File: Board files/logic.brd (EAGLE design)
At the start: 44.5 x 57.1 mm, 21 parts, among them U1 LD1117, U2 LM2662, U3 LD1085V

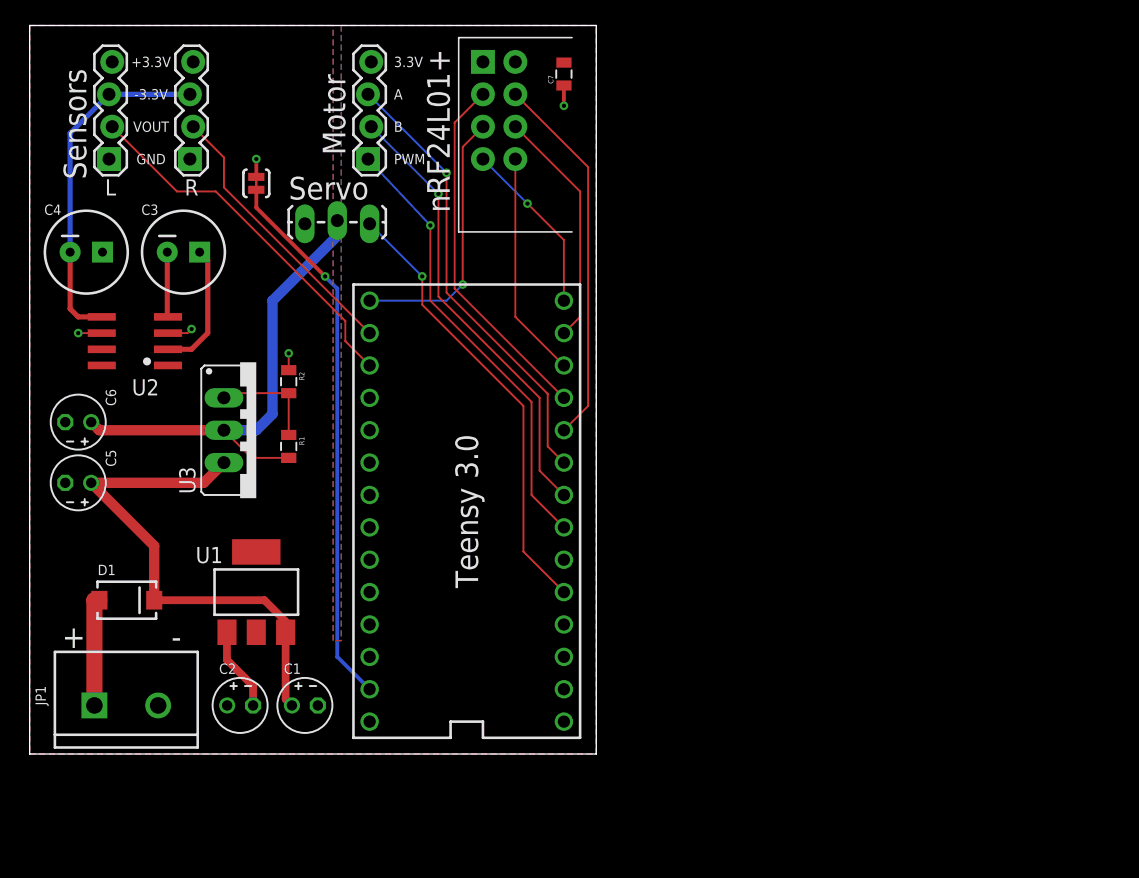
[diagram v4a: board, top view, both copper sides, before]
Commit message: Labels are no longer obscured by vias
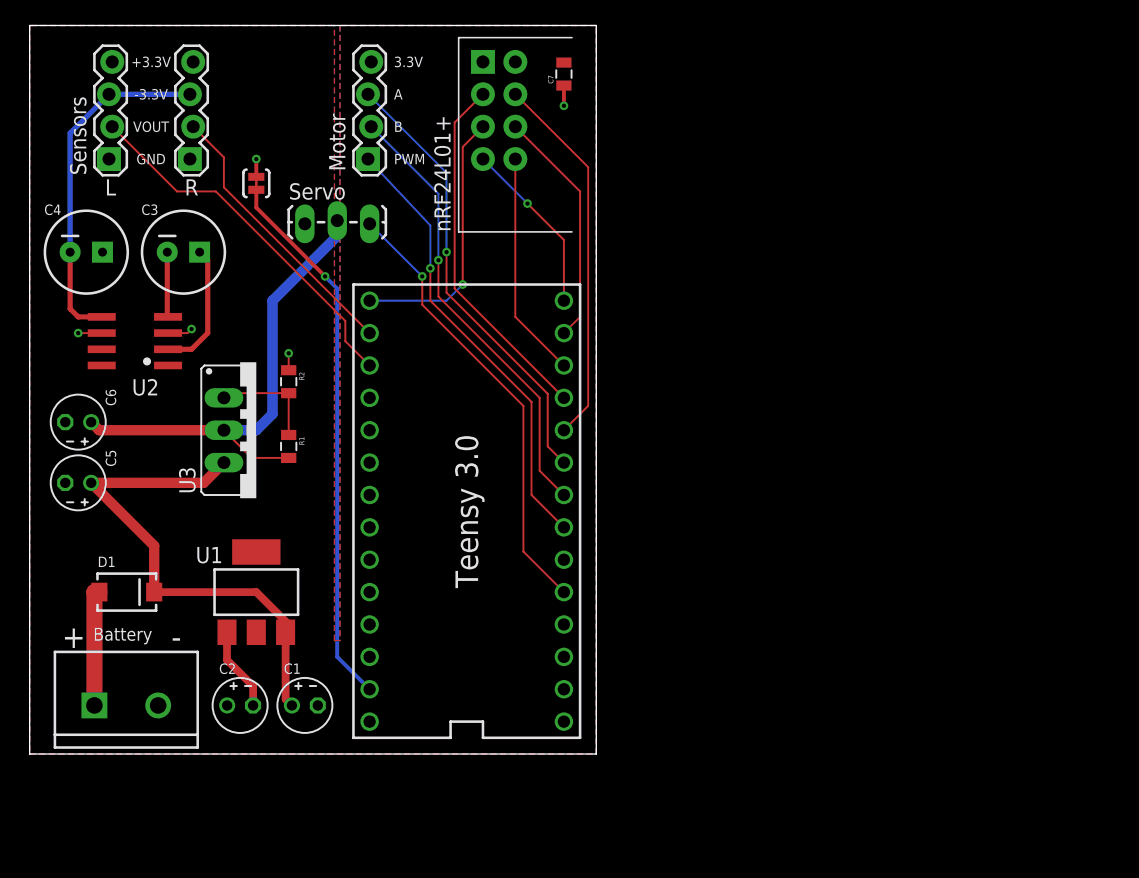
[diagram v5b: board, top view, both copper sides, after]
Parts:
- moved D1 0.63 mm to (7.62, 12.7)
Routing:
- net N$1: track 8.64 -> 9.28 mm
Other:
- board text added: "Battery"
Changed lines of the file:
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@@
 <text x="11.1125" y="9.2075" size="1.778" layer="21" align="center-left">-</text>
 <text x="34.29" y="19.05" size="1.778" layer="21" rot="R90" align="center">Teensy 3.0</text>
-<text x="32.0675" y="48.895" size="1.778" layer="21" rot="R90" align="center">nRF24L01+</text>
+<text x="33.02" y="40.9575" size="1.27" layer="21" rot="R90">nRF24L01+</text>
 <text x="9.525" y="46.6725" size="0.8128" layer="21" align="center">GND</text>
 <text x="9.525" y="49.2125" size="0.8128" layer="21" align="center">VOUT</text>
 <text x="9.525" y="51.7525" size="0.8128" layer="21" align="center">-3.3V</text>
 <text x="9.525" y="54.2925" size="0.8128" layer="21" align="center">+3.3V</text>
-<text x="4.445" y="45.085" size="1.778" layer="21" rot="R90">Sensors</text>
-<text x="20.32" y="43.4975" size="1.778" layer="21">Servo</text>
-<text x="24.765" y="46.99" size="1.778" layer="21" rot="R90">Motor</text>
+<text x="4.445" y="45.4025" size="1.27" layer="21" rot="R90">Sensors</text>
+<text x="20.32" y="43.4975" size="1.27" layer="21">Servo</text>
+<text x="24.765" y="45.72" size="1.27" layer="21" rot="R90">Motor</text>
 <text x="6.35" y="45.085" size="1.27" layer="21" align="top-center">L</text>
 <text x="12.7" y="45.085" size="1.27" layer="21" align="top-center">R</text>
+<text x="7.3025" y="8.89" size="1.016" layer="21" align="bottom-center">Battery</text>
 </plain>
 <attributes>
@@
 </autorouter>
 <elements>
-<element name="D1" library="SparkFun-DiscreteSemi" package="SMA-DIODE" value="" x="7.62" y="12.065" smashed="yes">
-<attribute name="NAME" x="5.334" y="14.0335" size="0.8128" layer="25"/>
-<attribute name="VALUE" x="7.874" y="13.716" size="0.4064" layer="27"/>
+<element name="D1" library="SparkFun-DiscreteSemi" package="SMA-DIODE" value="" x="7.62" y="12.7" smashed="yes">
+<attribute name="NAME" x="5.334" y="14.6685" size="0.8128" layer="25"/>
+<attribute name="VALUE" x="7.874" y="14.351" size="0.4064" layer="27"/>
 </element>
 <element name="U1" library="Custom" package="SOT-223" value="LD1117" x="17.78" y="12.7" smashed="yes">
 <attribute name="NAME" x="13.0175" y="14.9733" size="1.27" layer="25"/>
 </element>
-<element name="JP1" library="SparkFun-Connectors" package="SCREWTERMINAL-5MM-2" value="M025MM" x="5.08" y="3.81" smashed="yes">
-<attribute name="NAME" x="1.27" y="3.81" size="0.8128" layer="25" rot="R90"/>
-</element>
+<element name="JP1" library="SparkFun-Connectors" package="SCREWTERMINAL-5MM-2" value="M025MM" x="5.08" y="3.81" smashed="yes"/>
 <element name="U3" library="v-reg" package="317TS" value="LD1085V" x="17.78" y="25.4" smashed="yes" rot="R270">
 <attribute name="NAME" x="11.7348" y="22.5425" size="1.27" layer="25" ratio="10" rot="R270"/>
@@
 <vertex x="44.45" y="0"/>
 <vertex x="44.45" y="57.15"/>
-<vertex x="24.4475" y="57.15"/>
-<vertex x="24.4475" y="8.89"/>
-<vertex x="23.8125" y="8.89"/>
-<vertex x="23.8125" y="57.15"/>
+<vertex x="24.35225" y="57.15"/>
+<vertex x="24.35225" y="8.89"/>
+<vertex x="23.90775" y="8.89"/>
+<vertex x="23.90775" y="57.15"/>
 <vertex x="0" y="57.15"/>
 </polygon>
@@
 <vertex x="44.45" y="0"/>
 <vertex x="44.45" y="57.15"/>
-<vertex x="24.4475" y="57.15"/>
-<vertex x="24.4475" y="8.89"/>
-<vertex x="23.8125" y="8.89"/>
-<vertex x="23.8125" y="57.15"/>
+<vertex x="24.35225" y="57.15"/>
+<vertex x="24.35225" y="8.89"/>
+<vertex x="23.90775" y="8.89"/>
+<vertex x="23.90775" y="57.15"/>
 <vertex x="0" y="57.15"/>
 </polygon>
@@
 <contactref element="C1" pad="+"/>
 <contactref element="C5" pad="+"/>
-<wire x1="9.77" y1="12.065" x2="9.77" y2="16.3285" width="0.8128" layer="1"/>
+<wire x1="9.77" y1="12.7" x2="9.77" y2="16.3285" width="0.8128" layer="1"/>
 <wire x1="20.08" y1="9.55" x2="20.08" y2="4.304" width="0.6096" layer="1"/>
 <wire x1="20.08" y1="4.304" x2="20.574" y2="3.81" width="0.6096" layer="1"/>
-<wire x1="9.77" y1="12.065" x2="18.415" y2="12.065" width="0.6096" layer="1"/>
-<wire x1="18.415" y1="12.065" x2="20.32" y2="10.16" width="0.6096" layer="1"/>
+<wire x1="9.77" y1="12.7" x2="17.78" y2="12.7" width="0.6096" layer="1"/>
+<wire x1="17.78" y1="12.7" x2="20.32" y2="10.16" width="0.6096" layer="1"/>
 <wire x1="20.32" y1="10.16" x2="20.32" y2="9.79" width="0.6096" layer="1"/>
 <wire x1="20.32" y1="9.79" x2="20.08" y2="9.55" width="0.6096" layer="1"/>
@@
 <contactref element="D1" pad="A"/>
 <contactref element="JP1" pad="1"/>
-<wire x1="5.08" y1="3.81" x2="5.08" y2="12.065" width="1.27" layer="1"/>
-<wire x1="5.08" y1="12.065" x2="5.47" y2="12.065" width="1.27" layer="1"/>
+<wire x1="5.08" y1="3.81" x2="5.08" y2="12.7" width="1.27" layer="1"/>
+<wire x1="5.08" y1="12.7" x2="5.47" y2="12.7" width="1.27" layer="1"/>
 </signal>
 <signal name="VNEG">
@@
 <wire x1="39.37" y1="20.32" x2="39.37" y2="27.6225" width="0.1524" layer="1"/>
 <wire x1="39.37" y1="27.6225" x2="31.4325" y2="35.56" width="0.1524" layer="1"/>
-<wire x1="31.4325" y1="35.56" x2="31.4325" y2="41.4655" width="0.1524" layer="1"/>
 <wire x1="31.4325" y1="41.4655" x2="26.543" y2="46.6725" width="0.1524" layer="16"/>
-<via x="31.4325" y="41.4655" extent="1-16" drill="0.3302"/>
+<wire x1="31.4325" y1="41.4655" x2="31.4325" y2="38.1" width="0.1524" layer="16"/>
+<via x="31.4325" y="38.1" extent="1-16" drill="0.3302"/>
+<wire x1="31.4325" y1="38.1" x2="31.4325" y2="35.56" width="0.1524" layer="1"/>
 </signal>
 <signal name="N$16">
@@
 <wire x1="40.005" y1="22.225" x2="40.005" y2="27.94" width="0.1524" layer="1"/>
 <wire x1="40.005" y1="27.94" x2="32.0675" y2="35.8775" width="0.1524" layer="1"/>
-<wire x1="32.0675" y1="35.8775" x2="32.0675" y2="43.942" width="0.1524" layer="1"/>
 <wire x1="32.0675" y1="43.942" x2="26.797" y2="49.2125" width="0.1524" layer="16"/>
-<via x="32.0675" y="43.942" extent="1-16" drill="0.3302"/>
+<wire x1="32.0675" y1="35.8775" x2="32.0675" y2="38.735" width="0.1524" layer="1"/>
+<via x="32.0675" y="38.735" extent="1-16" drill="0.3302"/>
+<wire x1="32.0675" y1="38.735" x2="32.0675" y2="43.942" width="0.1524" layer="16"/>
 </signal>
 <signal name="N$17">
@@
 <wire x1="40.64" y1="24.13" x2="40.64" y2="28.2575" width="0.1524" layer="1"/>
 <wire x1="40.64" y1="28.2575" x2="32.7025" y2="36.195" width="0.1524" layer="1"/>
-<wire x1="32.7025" y1="36.195" x2="32.7025" y2="45.593" width="0.1524" layer="1"/>
 <wire x1="32.7025" y1="45.593" x2="26.543" y2="51.7525" width="0.1524" layer="16"/>
-<via x="32.7025" y="45.593" extent="1-16" drill="0.3302"/>
+<wire x1="32.7025" y1="36.195" x2="32.7025" y2="39.37" width="0.1524" layer="1"/>
+<via x="32.7025" y="39.37" extent="1-16" drill="0.3302"/>
+<wire x1="32.7025" y1="39.37" x2="32.7025" y2="45.593" width="0.1524" layer="16"/>
 </signal>
 </signals>

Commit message: Minor logic board changes
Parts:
- turned R1 to 90 degrees
- turned R2 to 90 degrees
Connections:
- net 6V: now also R1.1; no longer R1.2
- net GND: now also R2.2; no longer R2.1
- net N$4: now also R1.2, R2.1; no longer R1.1, R2.2
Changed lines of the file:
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@@
 <text x="9.525" y="54.2925" size="0.8128" layer="21" align="center">+3.3V</text>
 <text x="4.445" y="45.4025" size="1.27" layer="21" rot="R90">Sensors</text>
-<text x="20.32" y="43.4975" size="1.27" layer="21">Servo</text>
+<text x="20.32" y="43.815" size="1.27" layer="21">Servo</text>
 <text x="24.765" y="45.72" size="1.27" layer="21" rot="R90">Motor</text>
 <text x="6.35" y="45.085" size="1.27" layer="21" align="top-center">L</text>
 <text x="12.7" y="45.085" size="1.27" layer="21" align="top-center">R</text>
-<text x="7.3025" y="8.89" size="1.016" layer="21" align="bottom-center">Battery</text>
+<text x="7.62" y="8.89" size="1.016" layer="21" align="bottom-center">Battery</text>
 </plain>
 <attributes>
@@
 </element>
 <element name="U1" library="Custom" package="SOT-223" value="LD1117" x="17.78" y="12.7" smashed="yes">
-<attribute name="NAME" x="13.0175" y="14.9733" size="1.27" layer="25"/>
+<attribute name="NAME" x="13.335" y="15.2908" size="1.27" layer="25"/>
 </element>
 <element name="JP1" library="SparkFun-Connectors" package="SCREWTERMINAL-5MM-2" value="M025MM" x="5.08" y="3.81" smashed="yes"/>
@@
 <attribute name="NAME" x="1.143" y="42.291" size="0.8128" layer="25"/>
 </element>
-<element name="R1" library="SparkFun-Resistors" package="0805" value="150" x="20.32" y="24.13" rot="R270"/>
-<element name="R2" library="SparkFun-Resistors" package="0805" value="562" x="20.32" y="29.21" rot="R270"/>
+<element name="R1" library="SparkFun-Resistors" package="0805" value="150" x="20.32" y="24.13" rot="R90"/>
+<element name="R2" library="SparkFun-Resistors" package="0805" value="562" x="20.32" y="29.21" rot="R90"/>
 <element name="C1" library="resistor" package="E2-4" value="10uF" x="21.59" y="3.81" smashed="yes">
 <attribute name="NAME" x="19.939" y="6.2865" size="0.8128" layer="25" ratio="10"/>
@@
 </element>
 <element name="C5" library="resistor" package="E2-4" value="10uF" x="3.81" y="21.2725" smashed="yes" rot="R180">
-<attribute name="NAME" x="5.969" y="23.876" size="0.8128" layer="25" ratio="10" rot="R270"/>
+<attribute name="NAME" x="0.889" y="20.066" size="0.8128" layer="25" ratio="10" rot="R270"/>
 </element>
 <element name="C6" library="resistor" package="E2-4" value="10uF" x="3.81" y="26.035" smashed="yes" rot="R180">
-<attribute name="NAME" x="5.969" y="28.6385" size="0.8128" layer="25" ratio="10" rot="R270"/>
+<attribute name="NAME" x="0.889" y="24.8285" size="0.8128" layer="25" ratio="10" rot="R270"/>
 </element>
 <element name="A2" library="Custom" package="NRF24L01+" value="NRF24L01+" x="36.83" y="50.4825" smashed="yes" rot="R270"/>
@@
 <contactref element="U2" pad="6"/>
 <contactref element="U2" pad="3"/>
-<contactref element="R2" pad="1"/>
+<contactref element="R2" pad="2"/>
 <contactref element="C1" pad="-"/>
 <contactref element="C2" pad="-"/>
@@
 <signal name="6V">
 <contactref element="U3" pad="2"/>
-<contactref element="R1" pad="2"/>
+<contactref element="R1" pad="1"/>
 <contactref element="C6" pad="+"/>
 <contactref element="SERVO" pad="2"/>
@@
 <signal name="N$4">
 <contactref element="U3" pad="1"/>
-<contactref element="R2" pad="2"/>
-<contactref element="R1" pad="1"/>
+<contactref element="R2" pad="1"/>
+<contactref element="R1" pad="2"/>
 <wire x1="20.32" y1="28.31" x2="20.32" y2="25.03" width="0.1524" layer="1"/>
 <wire x1="15.24" y1="27.94" x2="15.61" y2="28.31" width="0.1524" layer="1"/>
@@
 <wire x1="26.67" y1="30.48" x2="24.765" y2="32.385" width="0.1524" layer="1"/>
 <wire x1="24.765" y1="32.385" x2="24.765" y2="33.9725" width="0.1524" layer="1"/>
-<wire x1="24.765" y1="33.9725" x2="14.605" y2="44.1325" width="0.1524" layer="1"/>
-<wire x1="14.605" y1="44.1325" x2="11.557" y2="44.1325" width="0.1524" layer="1"/>
-<wire x1="11.557" y1="44.1325" x2="6.477" y2="49.2125" width="0.1524" layer="1"/>
+<wire x1="24.765" y1="33.9725" x2="13.335" y2="45.4025" width="0.1524" layer="1"/>
+<wire x1="13.335" y1="45.4025" x2="10.287" y2="45.4025" width="0.1524" layer="1"/>
+<wire x1="10.287" y1="45.4025" x2="6.477" y2="49.2125" width="0.1524" layer="1"/>
 </signal>
 <signal name="N$12">
@@
 <contactref element="A1" pad="14/A0"/>
 <contactref element="SENSOR_R" pad="2"/>
-<wire x1="26.67" y1="33.02" x2="15.24" y2="44.45" width="0.1524" layer="1"/>
-<wire x1="15.24" y1="44.45" x2="15.24" y2="46.7995" width="0.1524" layer="1"/>
-<wire x1="15.24" y1="46.7995" x2="12.827" y2="49.2125" width="0.1524" layer="1"/>
+<wire x1="26.67" y1="33.02" x2="13.843" y2="45.847" width="0.1524" layer="1"/>
+<wire x1="13.843" y1="45.847" x2="13.843" y2="48.1965" width="0.1524" layer="1"/>
+<wire x1="13.843" y1="48.1965" x2="12.827" y2="49.2125" width="0.1524" layer="1"/>
 </signal>
 <signal name="N$15">

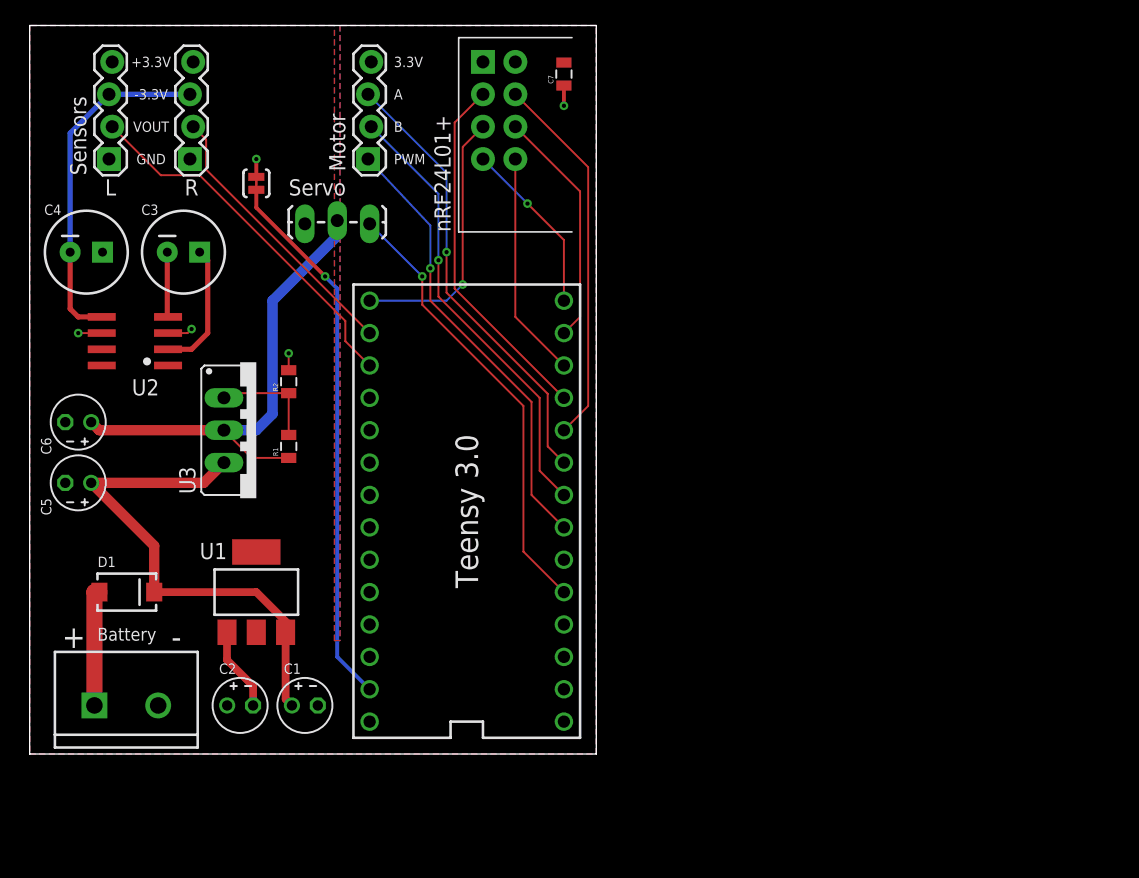
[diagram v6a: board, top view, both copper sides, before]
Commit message: Switched to polarized connectors
Also added 3.3v out pins on logic board, various other changes
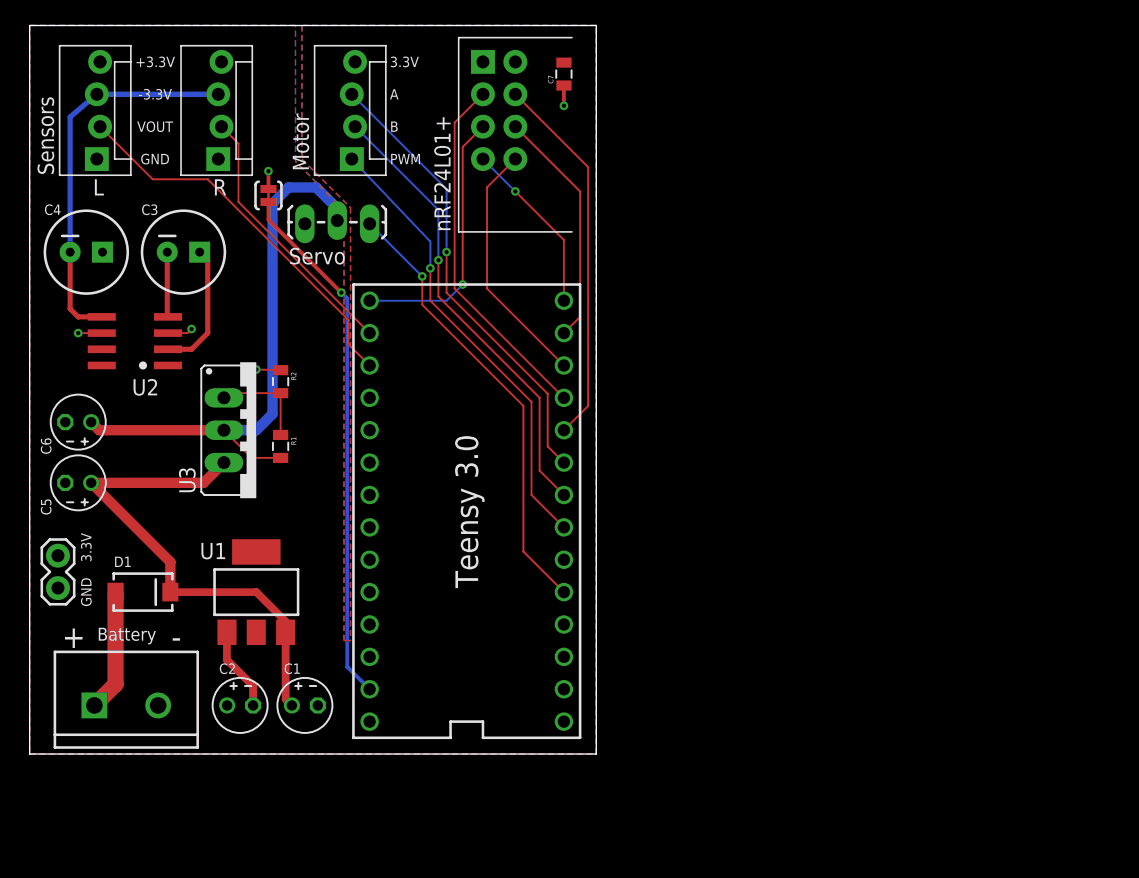
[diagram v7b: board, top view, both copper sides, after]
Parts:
- added JP2: M02PTH, SparkFun-Connectors:1X02
- MOTOR, SENSOR_L, SENSOR_R: device SparkFun-Connectors:1X04_LOCK -> SparkFun-Connectors:MOLEX-1X4_LOCK
- moved SENSOR_R 2.22 mm to (14.9, 46.7)
- moved SJ1 1.35 mm to (18.7, 43.8)
- moved MOTOR 1.27 mm to (25.4, 46.7)
- moved D1 1.27 mm to (8.89, 12.7)
- moved SENSOR_L 0.95 mm to (5.40, 46.7)
- moved R1 0.64 mm to (19.7, 24.1), turned to 270 degrees
- moved R2 0.64 mm to (19.7, 29.2), turned to 270 degrees
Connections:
- net 3.3V: now also JP2.2
- net 6V: now also R1.2; no longer R1.1
- net GND: now also JP2.1, R2.1; no longer R2.2
- net N$4: now also R1.1, R2.2; no longer R1.2, R2.1
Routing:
- net 6V: track 38.3 -> 44.1 mm
- net VNEG: track 27.2 -> 30.1 mm
- net N$9: track 17.8 -> 19.6 mm
- net N$12: track 42.9 -> 41.5 mm
- net N$13: track 28.9 -> 30.0 mm
- net N$14: track 21.9 -> 21.0 mm
- net V_BATT: track 39.9 -> 39.2 mm
- net N$4: track 8.51 -> 7.88 mm
- net GND: track 14.7 -> 15.3 mm
- net N$17: track 35.3 -> 35.8 mm
- net N$16: track 35.2 -> 35.7 mm
- net N$15: track 35.2 -> 35.7 mm
